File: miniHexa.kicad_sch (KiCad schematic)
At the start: 16 parts, among them U4 STM32F411CEUx, Y1 8Mhz

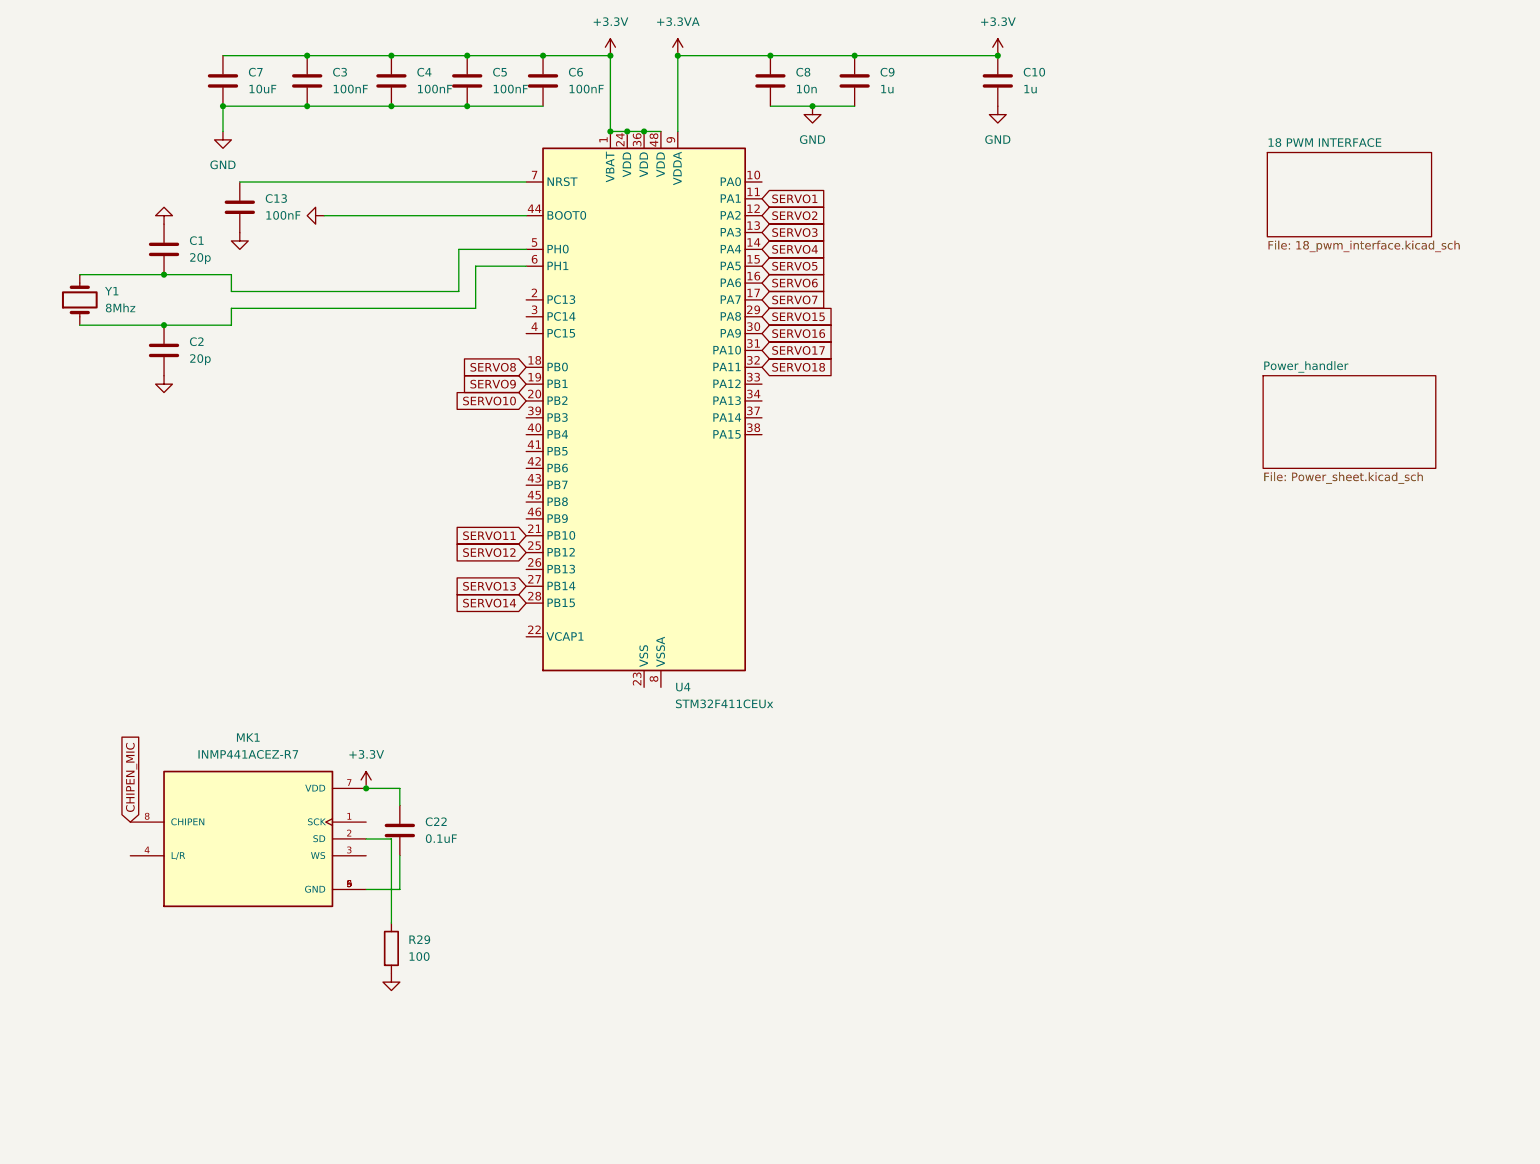
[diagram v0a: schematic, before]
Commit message: Updated schema
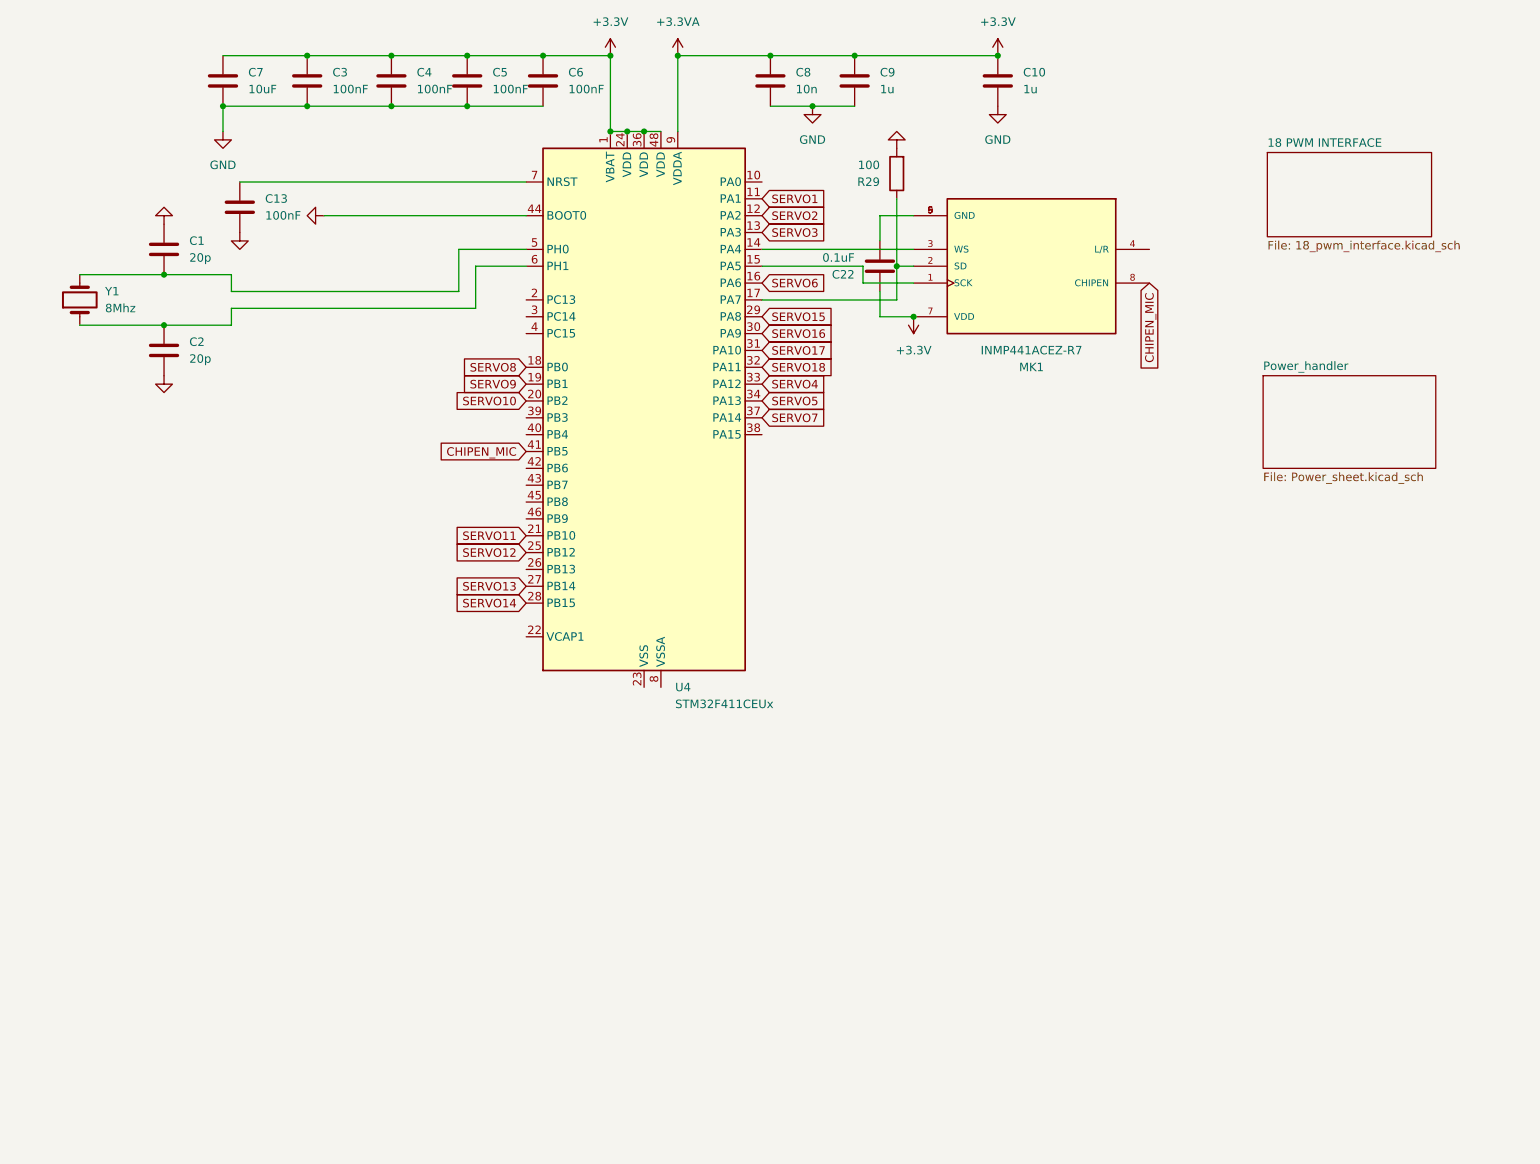
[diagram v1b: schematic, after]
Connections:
- net CHIPEN_MIC: now also U4.41 (PB5)
- net SERVO4: now also U4.33 (PA12); no longer U4.14 (PA4)
- net SERVO5: now also U4.34 (PA13); no longer U4.15 (PA5)
- net SERVO7: now also U4.37 (PA14); no longer U4.17 (PA7)
- net at MK1.1 (SCK): now also U4.15 (PA5)
- net at MK1.2 (SD), R29.1: now also U4.17 (PA7)
- net at MK1.3 (WS): now also U4.14 (PA4)
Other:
- moved on the sheet: C22, MK1, R29

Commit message: update -- i don't remeber what
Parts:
- Y1: value 8Mhz -> 16Mhz
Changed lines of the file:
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@@
 			)
 		)
-		(property "Value" "8Mhz"
+		(property "Value" "16Mhz"
 			(at 27.94 71.1199 90)
 			(effects

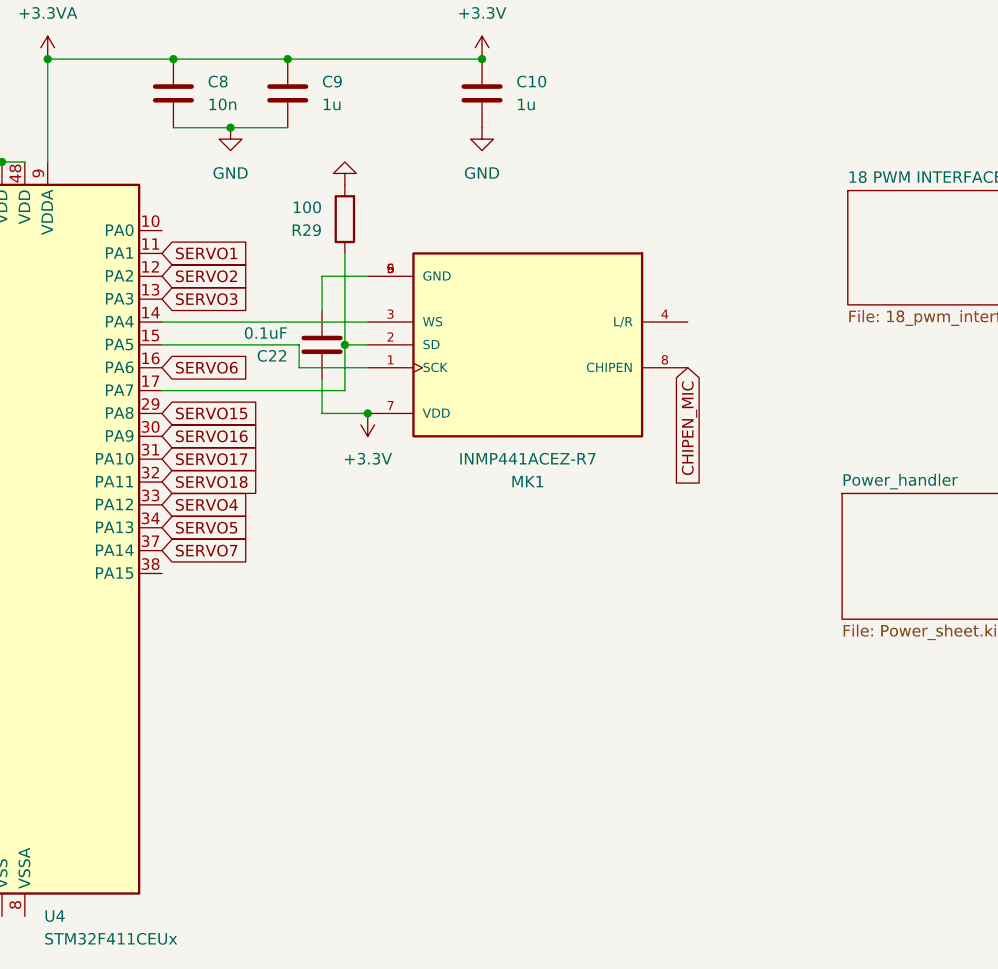
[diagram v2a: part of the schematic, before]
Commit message: moved firmware development to a different folder
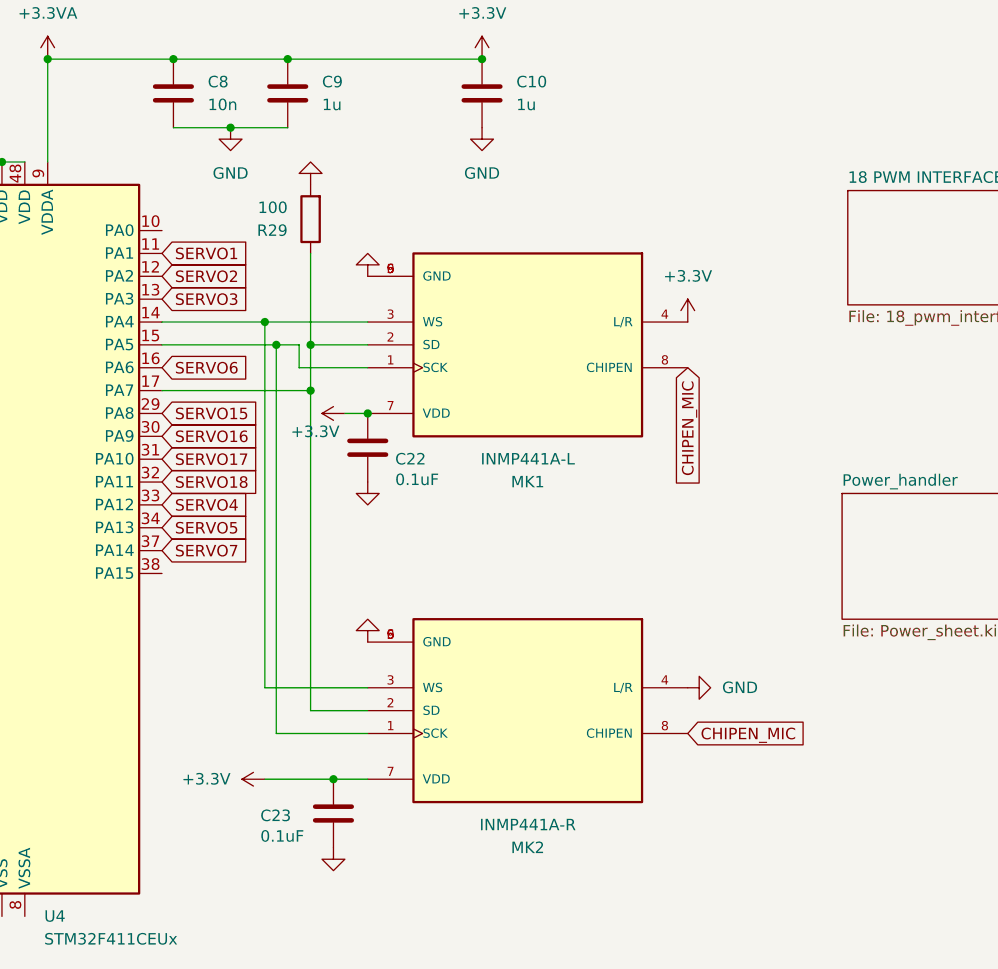
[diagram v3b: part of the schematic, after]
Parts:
- added C23: 0.1uF, Capacitor_SMD:C_0805_2012Metric, symbol Device:C
- added MK2: INMP441A-R, Microphone:MIC_INMP441ACEZ-R7, symbol Microphone:INMP441ACEZ-R7
- MK1: value INMP441ACEZ-R7 -> INMP441A-L
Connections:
- net +3.3V: now also MK1.4 (L/R), C23.1, MK2.7 (VDD)
- net CHIPEN_MIC: now also MK2.8 (CHIPEN)
- net GND: now also C22.2, MK1.5 (GND), MK1.6 (GND), MK1.9 (GND), C23.2, MK2.4 (L/R), MK2.5 (GND), MK2.6 (GND), MK2.9 (GND)
- net at MK1.1 (SCK), U4.15 (PA5): now also MK2.1 (SCK)
- net at MK1.2 (SD), R29.1, U4.17 (PA7): now also MK2.2 (SD)
- net at MK1.3 (WS), U4.14 (PA4): now also MK2.3 (WS)
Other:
- moved on the sheet: R29

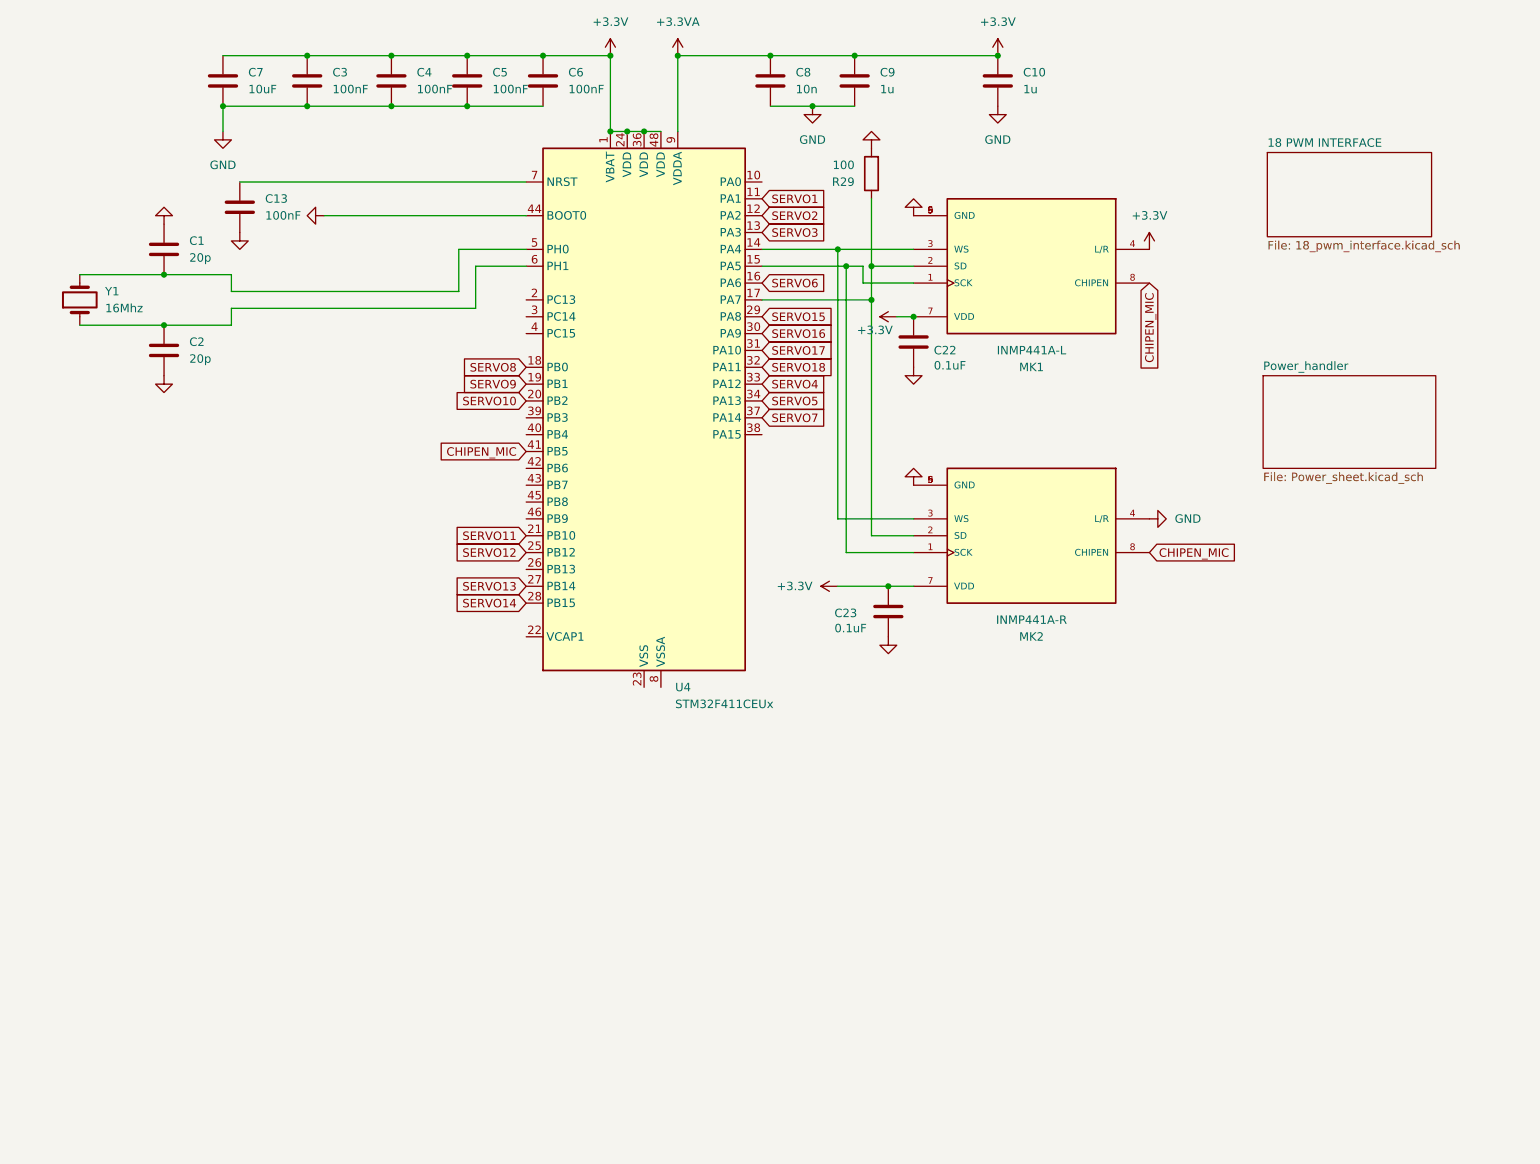
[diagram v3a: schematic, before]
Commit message: added stereo mics; cleaned up power management
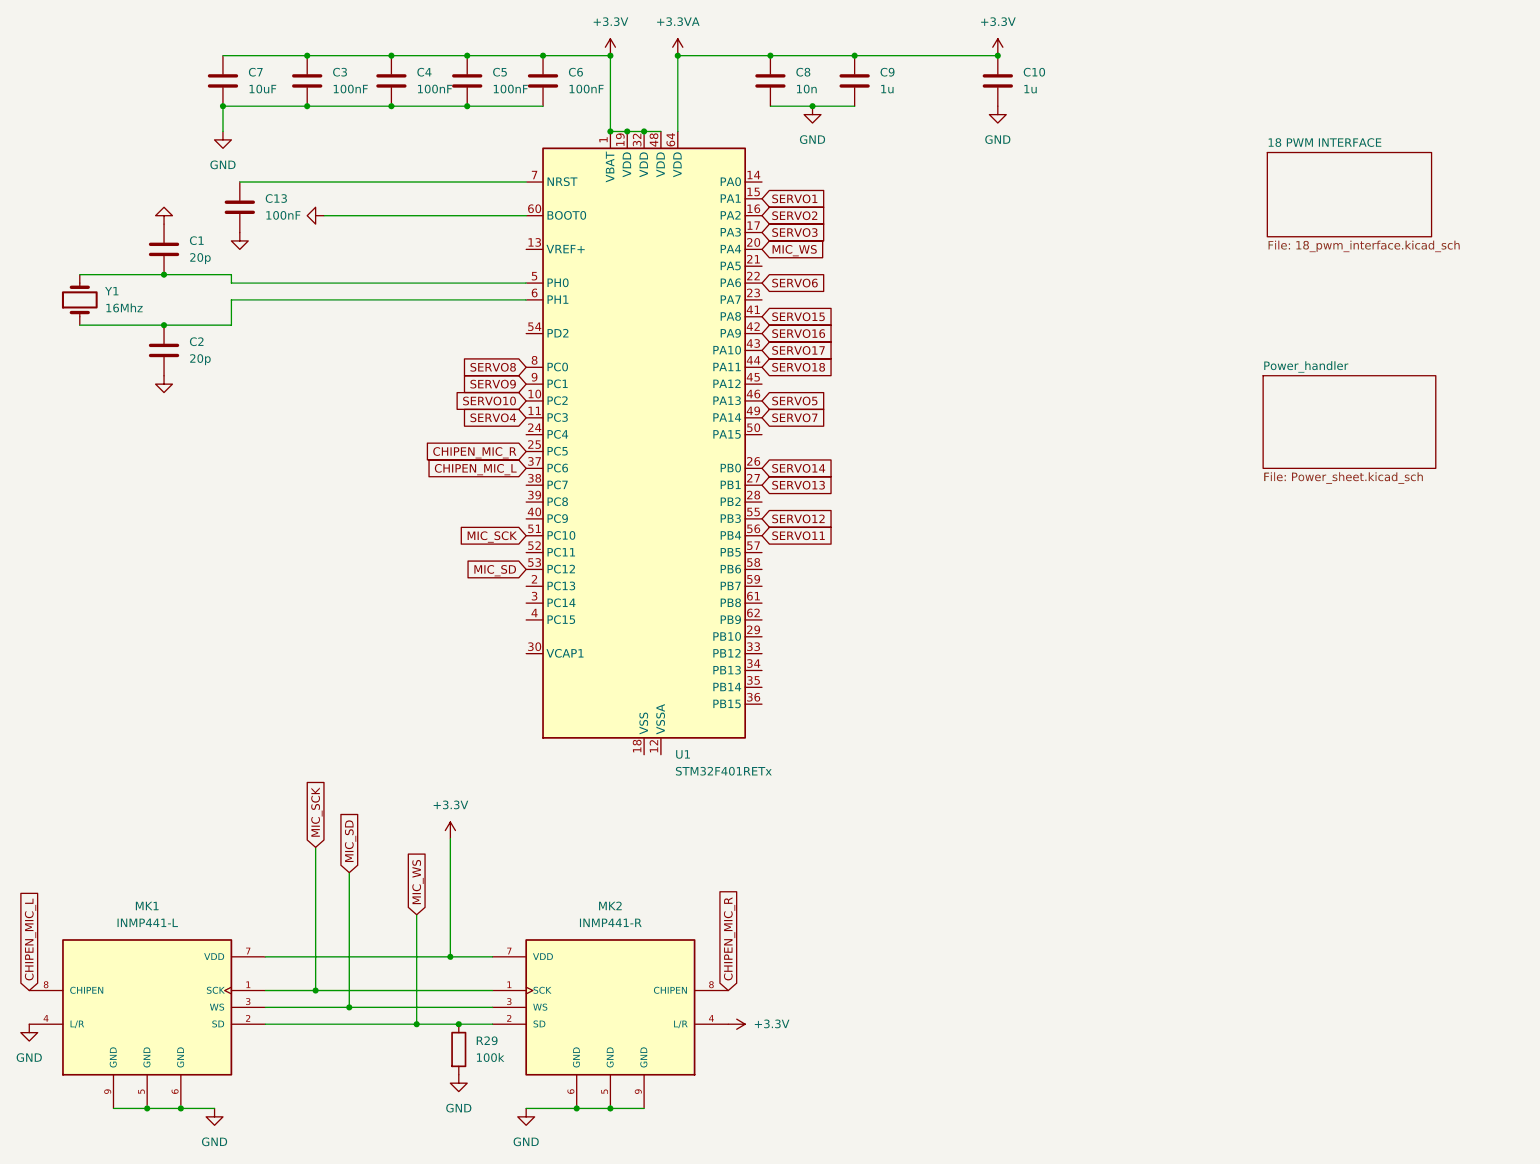
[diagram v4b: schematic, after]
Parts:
- removed C22, C23: 0.1uF, Capacitor_SMD:C_0805_2012Metric, symbol Device:C
- removed U4: STM32F411CEUx, Package_DFN_QFN:QFN-48-1EP_7x7mm_P0.5mm_EP5.6x5.6mm, symbol MCU_ST_STM32F4:STM32F411CEUx
- added U1: STM32F401RETx, Package_QFP:LQFP-64_10x10mm_P0.5mm, symbol MCU_ST_STM32F4:STM32F401RETx
- MK1: value INMP441A-L -> INMP441-L
- MK2: value INMP441A-R -> INMP441-R
- R29: value 100 -> 100k; footprint Resistor_SMD:R_0805_2012Metric -> (none)
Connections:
- net +3.3V: now also MK2.4 (L/R), U1.1 (VBAT), U1.19 (VDD), U1.32 (VDD), U1.48 (VDD), U1.64 (VDD); no longer MK1.4 (L/R)
- net GND: now also MK1.4 (L/R), U1.60 (BOOT0); no longer MK2.4 (L/R)
- net SERVO1: now also U1.15 (PA1)
- net SERVO10: now also U1.10 (PC2)
- net SERVO11: now also U1.56 (PB4)
- net SERVO12: now also U1.55 (PB3)
- net SERVO13: now also U1.27 (PB1)
- net SERVO14: now also U1.26 (PB0)
- net SERVO15: now also U1.41 (PA8)
- net SERVO16: now also U1.42 (PA9)
- net SERVO17: now also U1.43 (PA10)
- net SERVO18: now also U1.44 (PA11)
- net SERVO2: now also U1.16 (PA2)
- net SERVO3: now also U1.17 (PA3)
- net SERVO4: now also U1.11 (PC3)
- net SERVO5: now also U1.46 (PA13)
- net SERVO6: now also U1.22 (PA6)
- net SERVO7: now also U1.49 (PA14)
- net SERVO8: now also U1.8 (PC0)
- net SERVO9: now also U1.9 (PC1)
- net MIC_SCK: now reaches MK1.1 (SCK), MK2.1 (SCK)
- net MIC_SCK: now also U1.51 (PC10)
- net MIC_WS: now reaches MK1.2 (SD), MK2.2 (SD), R29.1
- net MIC_WS: now also U1.20 (PA4)
- net MIC_SD: now reaches MK1.3 (WS), MK2.3 (WS)
- net MIC_SD: now also U1.53 (PC12)
- net at C2.1, Y1.1: now also U1.6 (PH1)
- net at C1.2, Y1.2: now also U1.5 (PH0)
- net at C13.1: now also U1.7 (NRST)
- net CHIPEN_MIC renamed CHIPEN_MIC_L
- net CHIPEN_MIC_L: now also U1.37 (PC6); no longer MK2.8 (CHIPEN)
- new net: U1.18 (VSS), U1.31 (VSS), U1.47 (VSS), U1.63 (VSS)
- new net CHIPEN_MIC_R: MK2.8 (CHIPEN), U1.25 (PC5)
